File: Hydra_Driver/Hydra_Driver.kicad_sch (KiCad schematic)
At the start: 38 parts, among them IC1 ESP32-S3-WROOM-1-N4, J1 Conn_01x02, J2 Conn_01x02, J3 Conn_01x06, J4 Conn_01x06, J5 Conn_01x04, J6 Conn_01x04, J7 Conn_01x03, J8 Conn_01x03, J9 USB4105-GF-A, SW1 SW_SPST, SW2 SW_SPST, U1 MIC5365-3.3YC5, U2 USBLC6-2SC6

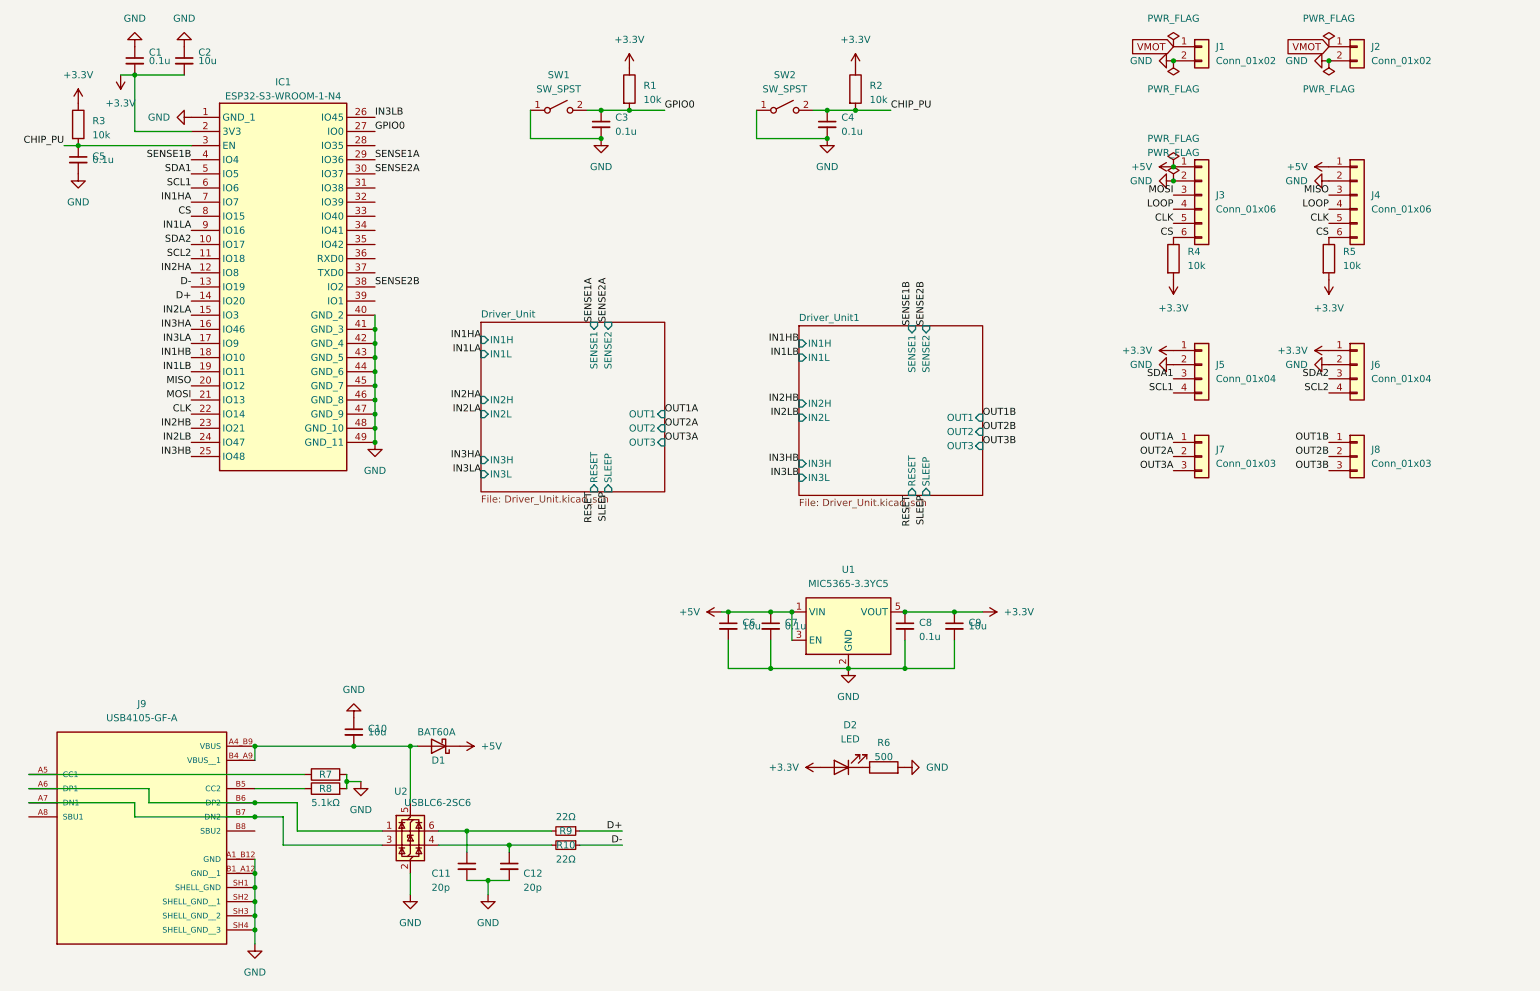
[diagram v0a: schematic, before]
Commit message: Finished general layout of hydra board
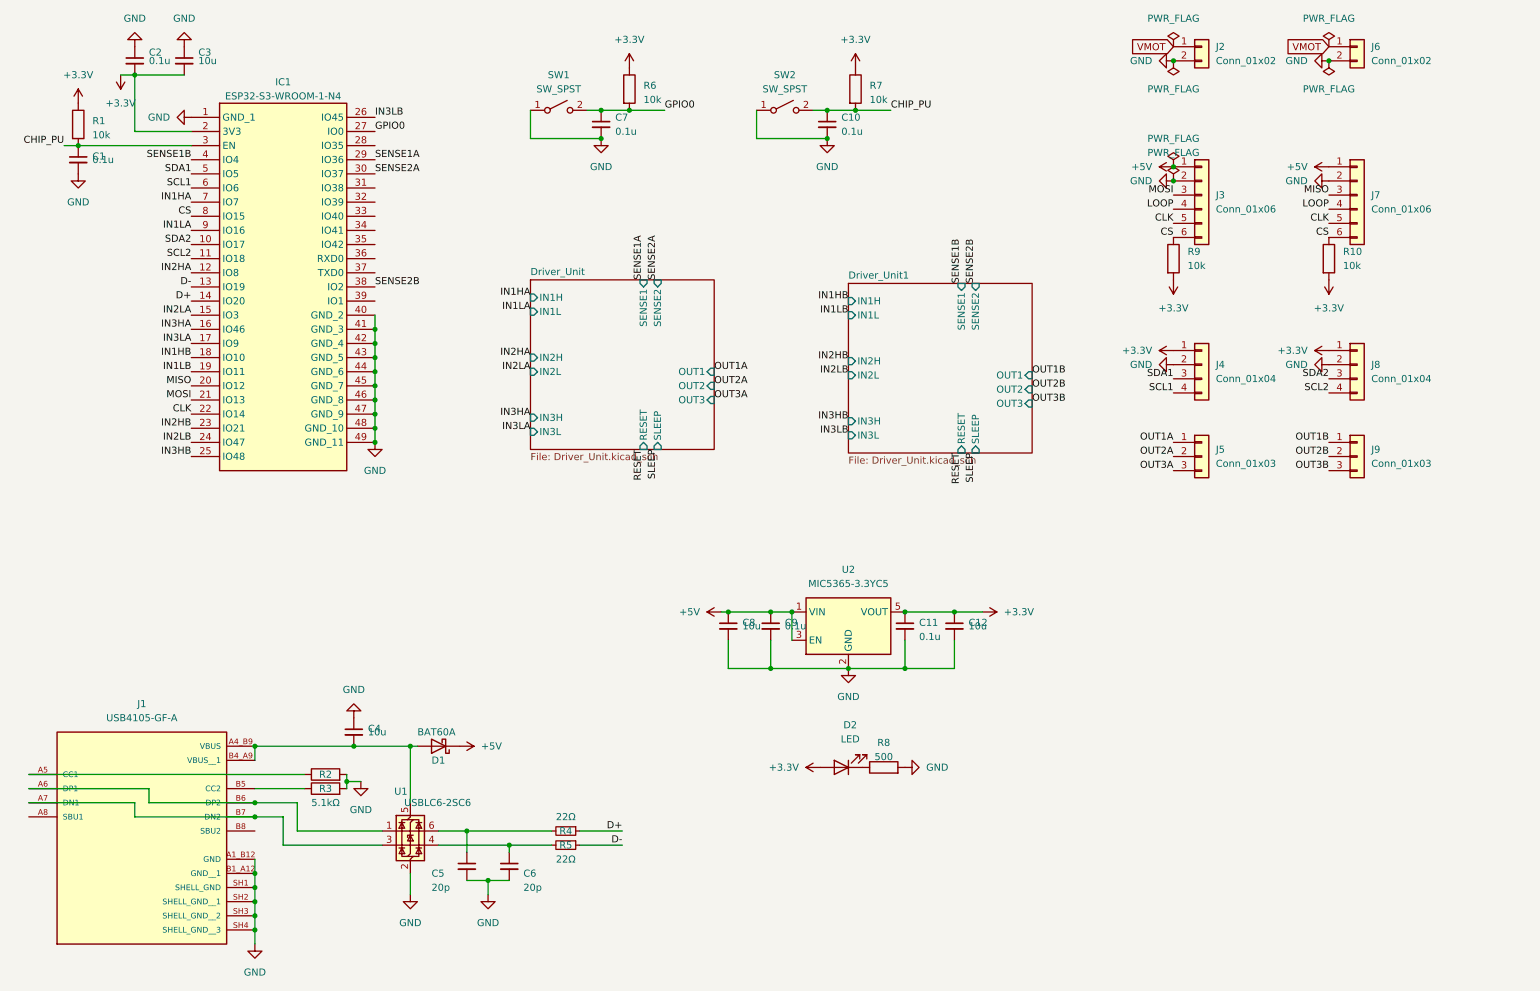
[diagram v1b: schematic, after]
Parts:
- renumbered C5 to C1, C4 to C10, C8 to C11, C9 to C12, C1 to C2, C2 to C3, C10 to C4, C11 to C5, C12 to C6, C3 to C7, C6 to C8, C7 to C9, J9 to J1, J1 to J2, J5 to J4, J7 to J5, J2 to J6, J4 to J7, J6 to J8, J8 to J9, R3 to R1, R5 to R10, R7 to R2, R8 to R3, R9 to R4, R10 to R5, R1 to R6, R2 to R7, R6 to R8, R4 to R9, U2 to U1, U1 to U2

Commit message: Component placement mostly finalized
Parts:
- removed R10: 10k, Resistor_SMD:R_0402_1005Metric, symbol Device:R
- added D3: LED, LED_SMD:LED_0603_1608Metric, symbol Device:LED
- added J10, J4, J8: Conn_01x03, Connector_PinSocket_2.54mm:PinSocket_1x03_P2.54mm_Vertical, symbol Connector_Generic:Conn_01x03
- added J7: Conn_01x02, Connector_PinSocket_2.54mm:PinSocket_1x02_P2.54mm_Vertical, symbol Connector_Generic:Conn_01x02
- added R9: 500, Resistor_SMD:R_0402_1005Metric, symbol Device:R
- renumbered J8 to J11, J9 to J12, J6 to J13, J4 to J5, J5 to J6, J7 to J9, R9 to R10
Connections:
- net +3.3V: now also D3.2 (A)
- net +5V: now also J3.6 (Pin_6), J9.6 (Pin_6), J8.2 (Pin_2); no longer J3.1 (Pin_1), J9.1 (Pin_1)
- net CLK: now also J3.2 (Pin_2), J9.2 (Pin_2), J10.2 (Pin_2), J4.2 (Pin_2); no longer J3.5 (Pin_5), J9.5 (Pin_5)
- net CS: now also J3.1 (Pin_1), J9.1 (Pin_1), J10.3 (Pin_3), J4.3 (Pin_3); no longer J3.6 (Pin_6), J9.6 (Pin_6)
- net GND: now also J3.5 (Pin_5), J9.5 (Pin_5), J8.3 (Pin_3), R9.2; no longer J3.2 (Pin_2), J9.2 (Pin_2)
- net IN1HA: now also IC1.11 (IO18); no longer IC1.7 (IO7)
- net IN1HB: now also IC1.23 (IO21); no longer IC1.18 (IO10)
- net IN1LA: now also IC1.15 (IO3); no longer IC1.9 (IO16)
- net IN1LB: now also IC1.24 (IO47); no longer IC1.19 (IO11)
- net IN2HA: now also IC1.16 (IO46); no longer IC1.12 (IO8)
- net IN2HB: now also IC1.25 (IO48); no longer IC1.23 (IO21)
- net IN2LA: now also IC1.17 (IO9); no longer IC1.15 (IO3)
- net IN2LB: now also IC1.26 (IO45); no longer IC1.24 (IO47)
- net IN3HA: now also IC1.18 (IO10); no longer IC1.16 (IO46)
- net IN3HB: now also IC1.28 (IO35); no longer IC1.25 (IO48)
- net IN3LA: now also IC1.19 (IO11); no longer IC1.17 (IO9)
- net IN3LB: now also IC1.29 (IO36); no longer IC1.26 (IO45)
- net MISO: now also J9.4 (Pin_4); no longer J9.3 (Pin_3)
- net MOSI: now also J3.4 (Pin_4); no longer J3.3 (Pin_3)
- net RESET: now also IC1.34 (IO41)
- net SCL1: now also IC1.31 (IO38); no longer IC1.6 (IO6)
- net SCL2: now also IC1.33 (IO40); no longer IC1.11 (IO18)
- net SDA1: now also IC1.30 (IO37); no longer IC1.5 (IO5)
- net SDA2: now also IC1.32 (IO39); no longer IC1.10 (IO17)
- net SENSE1A: now also IC1.6 (IO6); no longer IC1.29 (IO36)
- net SENSE1B: now also IC1.9 (IO16); no longer IC1.4 (IO4)
- net SENSE2A: now also IC1.7 (IO7); no longer IC1.30 (IO37)
- net SENSE2B: now also IC1.10 (IO17); no longer IC1.38 (IO2)
- net SLEEP: now also IC1.35 (IO42)
- net VMOT: now also J8.1 (Pin_1)
- removed net LOOP: J3.4 (Pin_4), J9.4 (Pin_4)
- new net: D3.1 (K), R9.1
- new net LED: IC1.38 (IO2)
- new net LOOP1: J3.3 (Pin_3), J4.1 (Pin_1), J7.1 (Pin_1)
- new net LOOP2: J10.1 (Pin_1), J7.2 (Pin_2), J9.3 (Pin_3)
- no-connect marks 0 -> 3
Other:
- moved on the sheet: J11, J12, J13, J2, J3, J5, J6, J9, R10

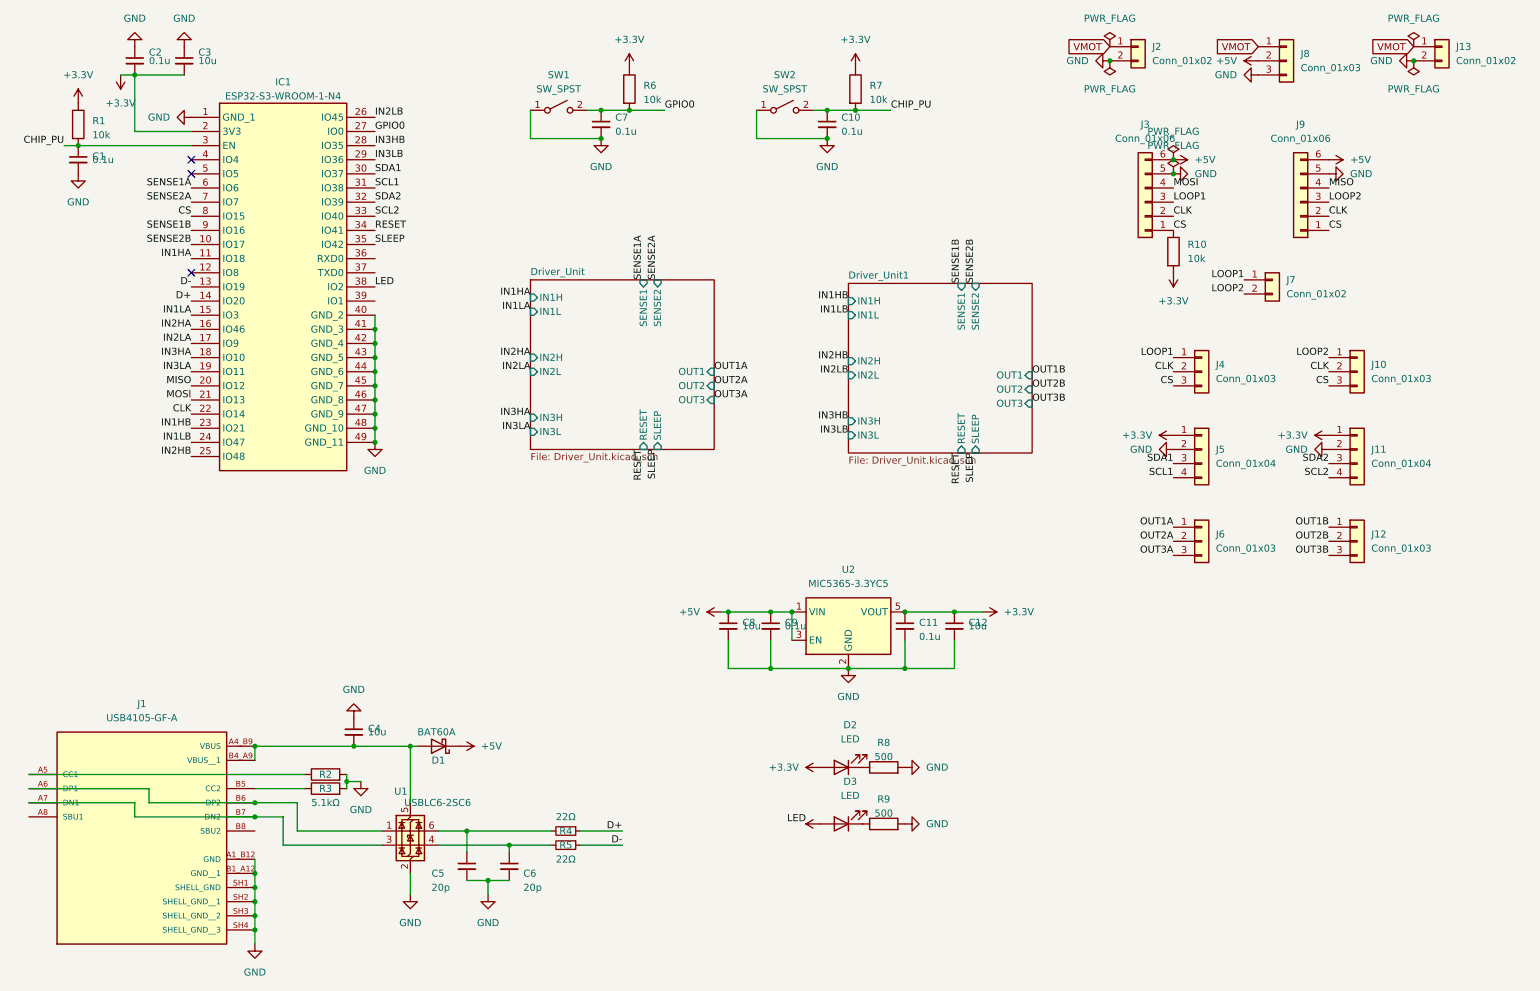
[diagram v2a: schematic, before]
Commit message: Finished layout for main hydra board
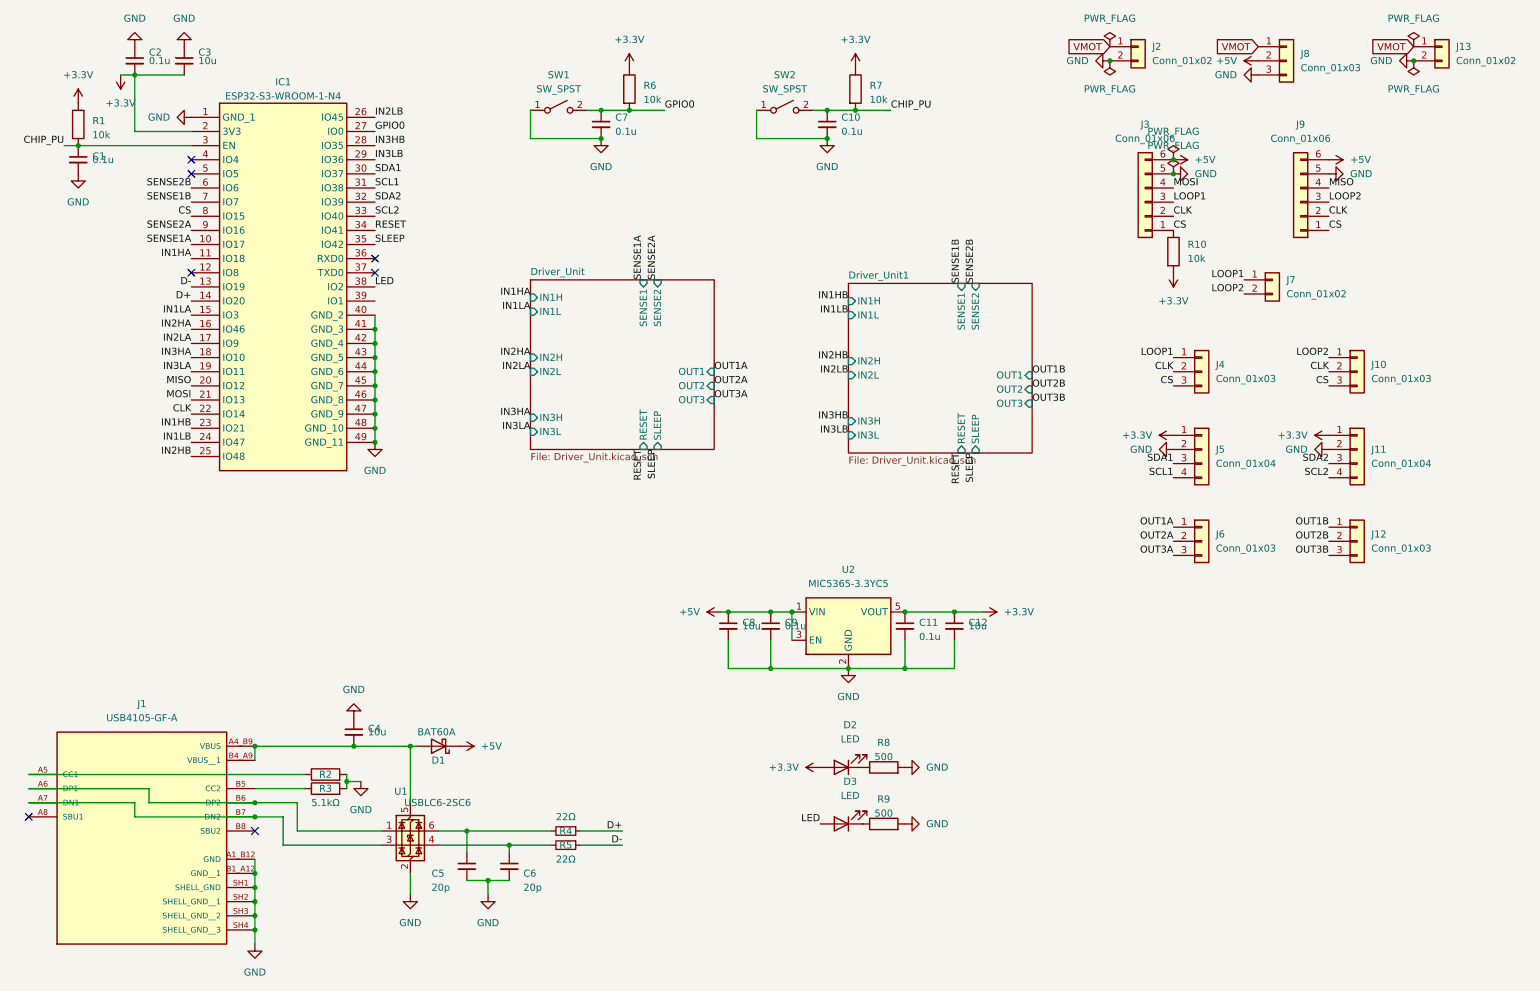
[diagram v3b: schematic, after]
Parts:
- R2: footprint Resistor_SMD:R_0402_1005Metric_Pad0.72x0.64mm_HandSolder -> Resistor_SMD:R_0402_1005Metric
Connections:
- net +3.3V: no longer D3.2 (A)
- net LED: now also D3.2 (A)
- net SENSE1A: now also IC1.10 (IO17); no longer IC1.6 (IO6)
- net SENSE1B: now also IC1.7 (IO7); no longer IC1.9 (IO16)
- net SENSE2A: now also IC1.9 (IO16); no longer IC1.7 (IO7)
- net SENSE2B: now also IC1.6 (IO6); no longer IC1.10 (IO17)
- no-connect marks 3 -> 7
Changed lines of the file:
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@@
 	)
 	(no_connect
+		(at 19.05 160.02)
+	)
+	(no_connect
+		(at 59.69 162.56)
+	)
+	(no_connect
+		(at 81.28 59.69)
+	)
+	(no_connect
 		(at 48.26 62.23)
 	)
 	(no_connect
+		(at 81.28 62.23)
+	)
+	(no_connect
 		(at 48.26 41.91)
 	)
@@
 	)
 	(label "SENSE1A"
-		(at 48.26 46.99 180)
+		(at 48.26 57.15 180)
 		(effects
 			(font
@@
 	)
 	(label "SENSE1B"
-		(at 48.26 54.61 180)
+		(at 48.26 49.53 180)
 		(effects
 			(font
@@
 	)
 	(label "LED"
-		(at 158.75 161.29 180)
+		(at 161.29 161.29 180)
 		(effects
 			(font
@@
 	)
 	(label "SENSE2A"
-		(at 48.26 49.53 180)
+		(at 48.26 54.61 180)
 		(effects
 			(font
@@
 	)
 	(label "SENSE2B"
-		(at 48.26 57.15 180)
+		(at 48.26 46.99 180)
 		(effects
 			(font
@@
 			)
 		)
-		(property "Footprint" "Resistor_SMD:R_0402_1005Metric_Pad0.72x0.64mm_HandSolder"
+		(property "Footprint" "Resistor_SMD:R_0402_1005Metric"
 			(at 72.39 154.178 90)
 			(effects
@@
 					(unit 1)
 				)
-			)
-		)
-	)
-	(symbol
-		(lib_name "+3.3V_1")
-		(lib_id "power:+3.3V")
-		(at 161.29 161.29 90)
-		(unit 1)
-		(exclude_from_sim no)
-		(in_bom yes)
-		(on_board yes)
-		(dnp no)
-		(fields_autoplaced yes)
-		(property "Reference" "#PWR018"
-			(at 165.1 161.29 0)
-			(effects
-				(font
-					(size 1.27 1.27)
-				)
-				(hide yes)
-			)
-		)
-		(property "Value" "+3.3V"
-			(at 157.48 161.2899 90)
-			(effects
-				(font
-					(size 1.27 1.27)
-				)
-				(justify left)
-				(hide yes)
-			)
-		)
-		(property "Footprint" ""
-			(at 161.29 161.29 0)
-			(effects
-				(font
-					(size 1.27 1.27)
-				)
-				(hide yes)
-			)
-		)
-		(property "Datasheet" ""
-			(at 161.29 161.29 0)
-			(effects
-				(font
-					(size 1.27 1.27)
-				)
-				(hide yes)
-			)
-		)
-		(property "Description" "Power symbol creates a global label with name \"+3.3V\""
-			(at 161.29 161.29 0)
-			(effects
-				(font
-					(size 1.27 1.27)
-				)
-				(hide yes)
-			)
-		)
-		(pin "1"
-		)
-		(instances
-			(project "Hydra_Driver"
-				(path "/c6ac9bb7-6504-498f-96ad-01ea1a04d6e7"
-					(reference "#PWR018")
-					(unit 1)
-				)

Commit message: Added silkscreen
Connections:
- net SCL1: now also IC1.33 (IO40), J11.4 (Pin_4); no longer IC1.31 (IO38), J5.4 (Pin_4)
- net SCL2: now also IC1.31 (IO38), J5.4 (Pin_4); no longer IC1.33 (IO40), J11.4 (Pin_4)
- net SDA1: now also IC1.32 (IO39), J11.3 (Pin_3); no longer IC1.30 (IO37), J5.3 (Pin_3)
- net SDA2: now also IC1.30 (IO37), J5.3 (Pin_3); no longer IC1.32 (IO39), J11.3 (Pin_3)
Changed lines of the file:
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@@
 		)
 	)
-	(label "SDA1"
+	(label "SDA2"
 		(at 81.28 44.45 0)
 		(effects
@@
 		)
 	)
-	(label "SCL1"
+	(label "SCL2"
 		(at 81.28 46.99 0)
 		(effects
@@
 		)
 	)
-	(label "SDA2"
+	(label "SDA1"
 		(at 252.73 96.52 180)
 		(effects
@@
 		)
 	)
-	(label "SCL1"
+	(label "SCL2"
 		(at 224.79 99.06 180)
 		(effects
@@
 		)
 	)
-	(label "SDA2"
+	(label "SDA1"
 		(at 81.28 49.53 0)
 		(effects
@@
 		)
 	)
-	(label "SDA1"
+	(label "SDA2"
 		(at 224.79 96.52 180)
 		(effects
@@
 		)
 	)
-	(label "SCL2"
+	(label "SCL1"
 		(at 81.28 52.07 0)
 		(effects
@@
 		)
 	)
-	(label "SCL2"
+	(label "SCL1"
 		(at 252.73 99.06 180)
 		(effects
